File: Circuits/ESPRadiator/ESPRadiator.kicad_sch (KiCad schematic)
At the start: 51 parts, among them Q1 AO3401A, Q3 IRLZ44N, Q4 IRLZ44N, U1 AP63203WU, U2 LTV-827S, U3 TC4427xOA

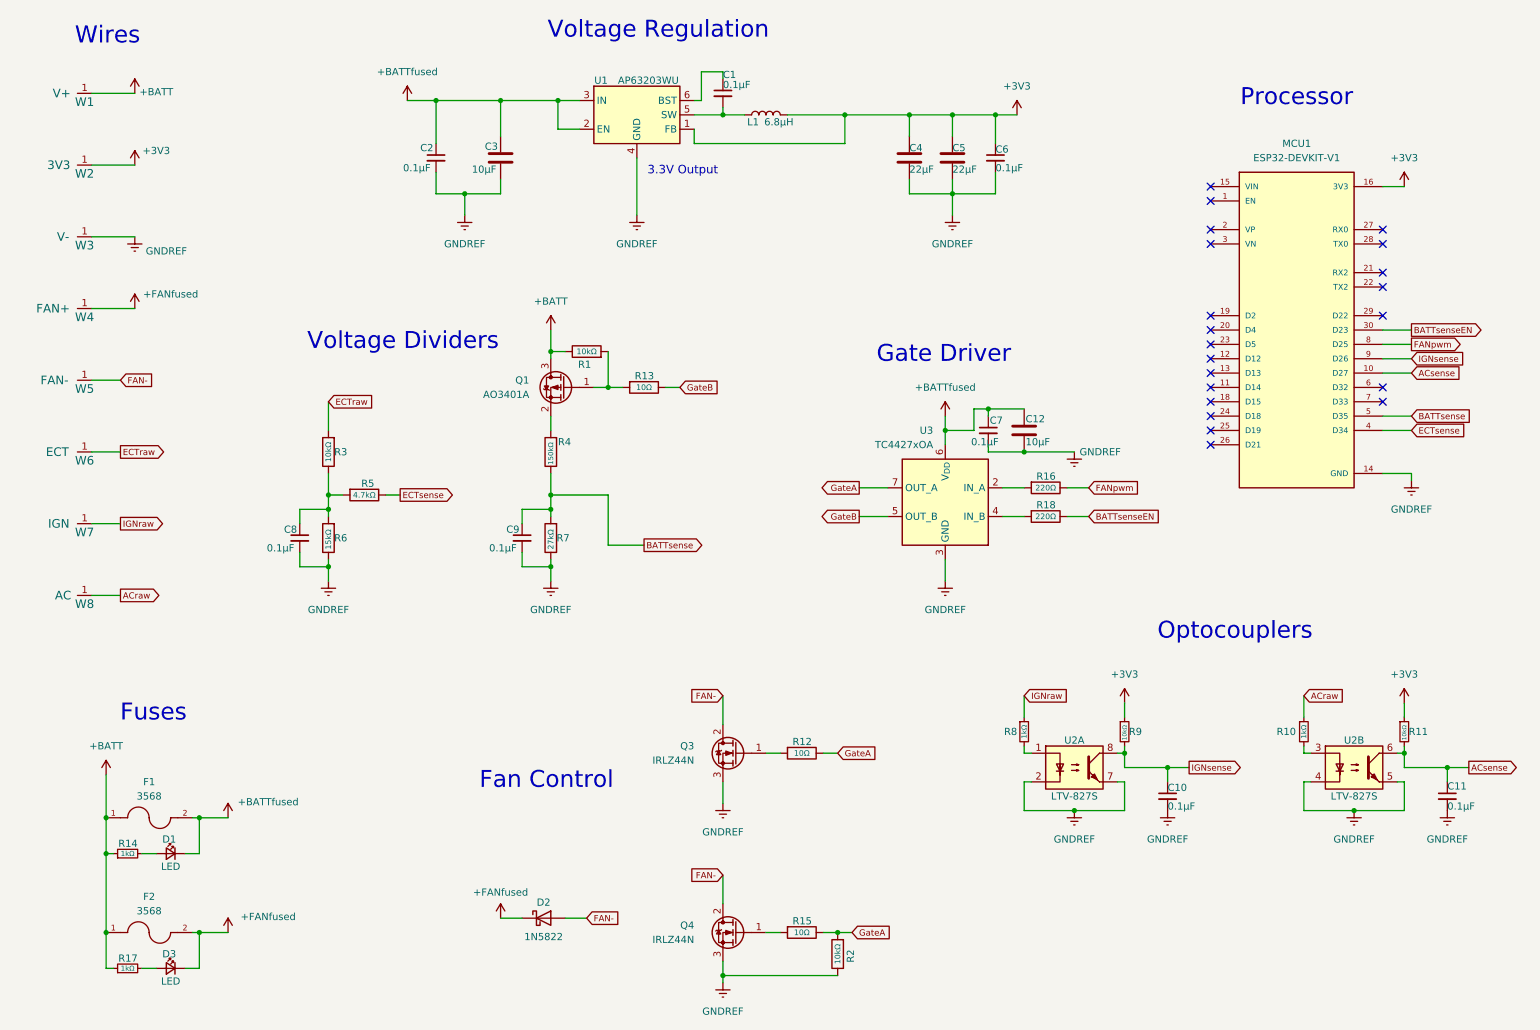
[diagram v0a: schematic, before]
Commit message: Major fertilator update, tweaks to ESPRadiator for gate controller
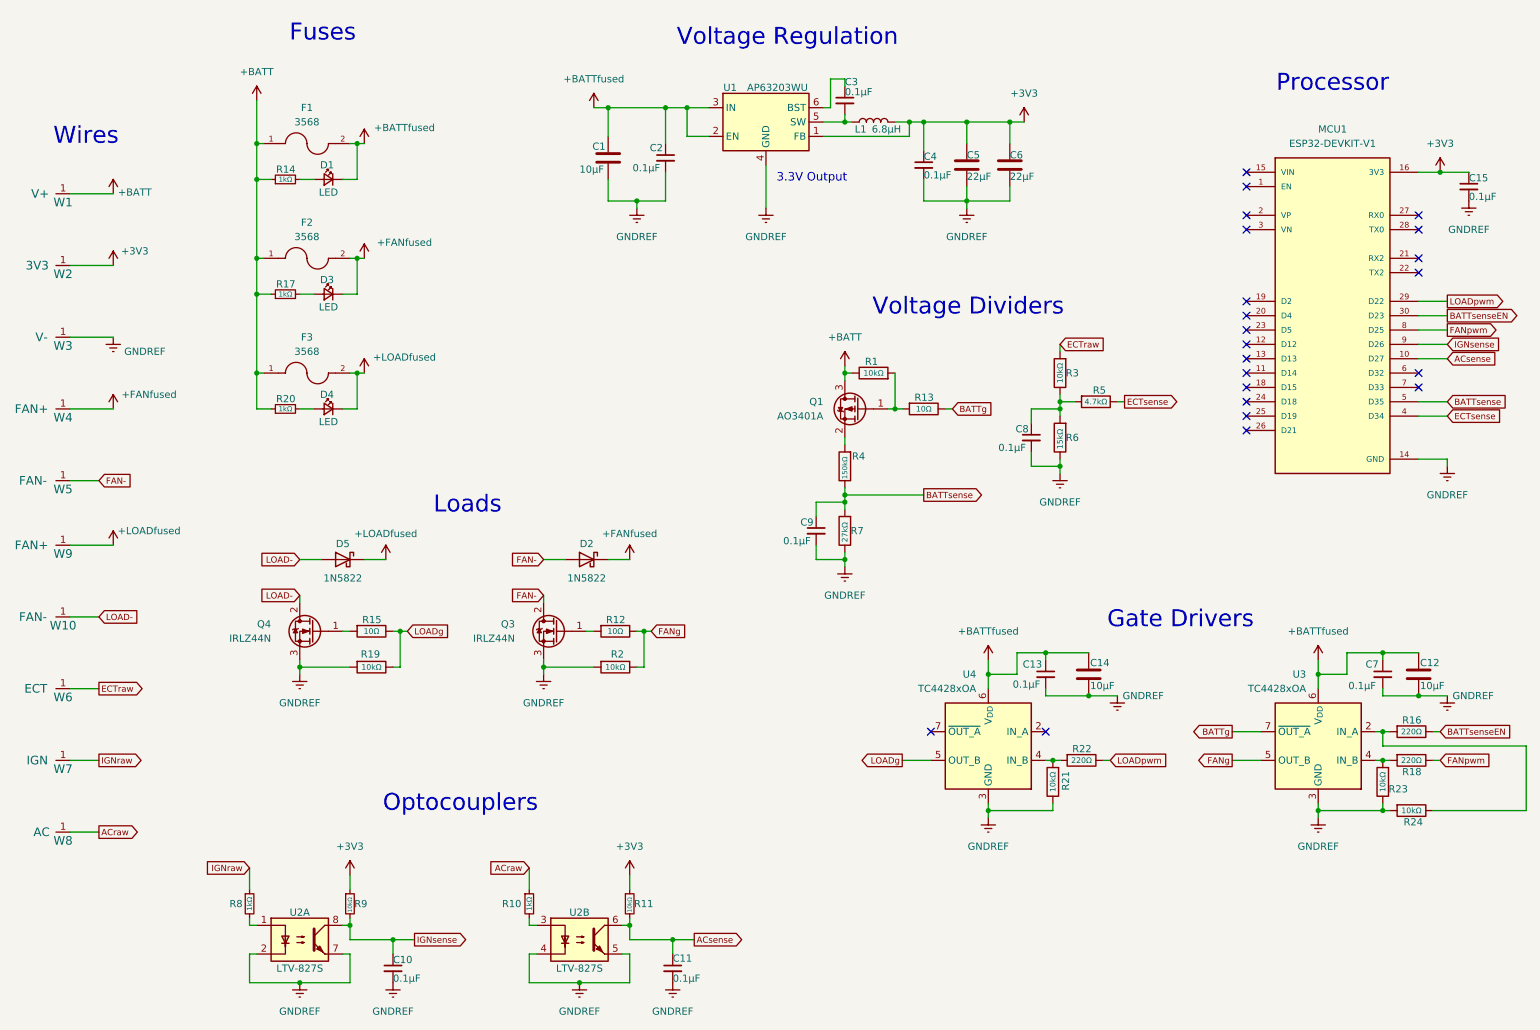
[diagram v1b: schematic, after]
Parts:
- added C13, C15: 0.1μF, Capacitor_SMD:C_0805_2012Metric_Pad1.18x1.45mm_HandSolder, symbol Device:C_Small
- added C14: 10μF, Capacitor_SMD:C_1206_3216Metric_Pad1.33x1.80mm_HandSolder, symbol Device:C
- added D4: LED, LED_SMD:LED_1206_3216Metric_Pad1.42x1.75mm_HandSolder, symbol Device:LED_Small
- added D5: 1N5822, Diode_THT:D_DO-201AD_P15.24mm_Horizontal, symbol Diode:1N5822
- added F3: 3568, Ehryk:FUSE_3568, symbol Ehryk:3568
- added R19, R21, R23, R24: 10kΩ, Resistor_SMD:R_0805_2012Metric_Pad1.20x1.40mm_HandSolder, symbol Device:R
- added R20: 1kΩ, Resistor_SMD:R_0805_2012Metric_Pad1.20x1.40mm_HandSolder, symbol Device:R_Small
- added R22: 220Ω, Resistor_SMD:R_0805_2012Metric_Pad1.20x1.40mm_HandSolder, symbol Device:R
- added U4: TC4428xOA, Package_SO:SOIC-8_3.9x4.9mm_P1.27mm, symbol Driver_FET:TC4428xOA
- added W10: FAN-, Ehryk:WIRE-10AWG, symbol Ehryk:WIRE
- added W9: FAN+, Ehryk:WIRE-10AWG, symbol Ehryk:WIRE
- U3: value TC4427xOA -> TC4428xOA; symbol Driver_FET:TC4427xOA -> Driver_FET:TC4428xOA
- renumbered C3 to C1, C1 to C3, C6 to C4, C4 to C6
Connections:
- net +3V3: now also C15.1
- net +BATT: now also F3.1, F3.3, R20.1
- net +BATTfused: now also C13.1, C14.2, U4.6 (V_{DD})
- net BATTsenseEN: now also R16.1; no longer R18.1
- net FAN-: no longer Q4.2 (D)
- net FANpwm: now also R18.1; no longer R16.1
- net GND: now also R2.2, C13.2, C14.1, C15.2, R19.2, R21.1, R23.1, R24.2, U4.3 (GND); no longer R2.1
- net at R18.2, U3.4 (IN_B): now also R23.2
- net at R16.2, U3.2 (IN_A): now also R24.1
- net LOADpwm: now reaches MCU1.29 (D22)
- net LOADpwm: now also R22.1
- removed net GateA: R12.1, R15.1, R2.2, U3.7 (OUT_A)
- net GateB renamed BATTg
- net BATTg: now also U3.7 (~{OUT_A}); no longer U3.5 (OUT_B)
- new net: R21.2, R22.2, U4.4 (IN_B)
- new net: D4.2 (A), R20.2
- new net +LOADfused: D4.1 (K), D5.1 (K), F3.2, F3.4, W9.1
- new net FANg: R12.1, R2.1, U3.5 (OUT_B)
- new net LOAD-: D5.2 (A), Q4.2 (D), W10.1
- new net LOADg: R15.1, R19.1, U4.5 (OUT_B)
- no-connect marks 21 -> 22
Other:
- note added: "Gate Drivers"
- note added: "Loads"
- note removed: "Fan Control"
- note removed: "Gate Driver"
- moved on the sheet: C1, C10, C11, C12, C2, C3, C4, C5, C6, C7, C8, C9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
